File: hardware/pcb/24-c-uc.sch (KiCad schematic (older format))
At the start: 4 parts

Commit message: Changed uC
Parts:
- removed U?: STM32L031K6Tx, Package_QFP:LQFP-32_7x7mm_P0.8mm, symbol MCU_ST_STM32L0:STM32L031K6Tx
- added C? (x3): 100nF, C0603, symbol Device:C
- added U?: STM32L151C8T6, Package_QFP:LQFP-48_7x7mm_P0.5mm, symbol MCU_ST_STM32L1:STM32L151C8Tx
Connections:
- net labels added: uC-Debug-Rx, uC-Debug-Tx
- wire segments 45 -> 85
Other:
- note added: "Add connector for Debug UART"
- note added: "Check caps"
- moved on the sheet: C?

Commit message: Created variants
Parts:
- gave numbers to parts that had none: 7
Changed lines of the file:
@@
 EESchema Schematic File Version 4
-EELAYER 30 0
+LIBS:24-clocks-cache
+EELAYER 29 0
 EELAYER END
 $Descr A4 11693 8268
@@
 P 5250 1400
 AR Path="/5FDEDBF8" Ref="#PWR?"  Part="1"
-AR Path="/5FDEAABE/5FDEDBF8" Ref="#PWR?"  Part="1"
-F 0 "#PWR?" H 5250 1250 50  0001 C CNN
+AR Path="/5FDEAABE/5FDEDBF8" Ref="#PWR0201"  Part="1"
+F 0 "#PWR0201" H 5250 1250 50  0001 C CNN
 F 1 "+3V3" H 5265 1573 50  0000 C CNN
 F 2 "" H 5250 1400 50  0001 C CNN
@@
 P 5250 4800
 AR Path="/5FDEDBFE" Ref="#PWR?"  Part="1"
-AR Path="/5FDEAABE/5FDEDBFE" Ref="#PWR?"  Part="1"
-F 0 "#PWR?" H 5250 4550 50  0001 C CNN
+AR Path="/5FDEAABE/5FDEDBFE" Ref="#PWR0202"  Part="1"
+F 0 "#PWR0202" H 5250 4550 50  0001 C CNN
 F 1 "GND" H 5255 4627 50  0000 C CNN
 F 2 "" H 5250 4800 50  0001 C CNN
@@
 P 4400 6500
 AR Path="/5FDEDC0A" Ref="C?"  Part="1"
-AR Path="/5FDEAABE/5FDEDC0A" Ref="C?"  Part="1"
-F 0 "C?" H 4515 6546 50  0000 L CNN
+AR Path="/5FDEAABE/5FDEDC0A" Ref="C201"  Part="1"
+F 0 "C201" H 4515 6546 50  0000 L CNN
 F 1 "100nF" H 4515 6455 50  0000 L CNN
 F 2 "C0603" H 4438 6350 50  0001 C CNN
@@
 P 4400 6800
 AR Path="/5FDEDC10" Ref="#PWR?"  Part="1"
-AR Path="/5FDEAABE/5FDEDC10" Ref="#PWR?"  Part="1"
-F 0 "#PWR?" H 4400 6550 50  0001 C CNN
+AR Path="/5FDEAABE/5FDEDC10" Ref="#PWR0207"  Part="1"
+F 0 "#PWR0207" H 4400 6550 50  0001 C CNN
 F 1 "GND" H 4405 6627 50  0000 C CNN
 F 2 "" H 4400 6800 50  0001 C CNN
@@
 P 4400 6200
 AR Path="/5FDEDC16" Ref="#PWR?"  Part="1"
-AR Path="/5FDEAABE/5FDEDC16" Ref="#PWR?"  Part="1"
-F 0 "#PWR?" H 4400 6050 50  0001 C CNN
+AR Path="/5FDEAABE/5FDEDC16" Ref="#PWR0204"  Part="1"
+F 0 "#PWR0204" H 4400 6050 50  0001 C CNN
 F 1 "+3V3" H 4415 6373 50  0000 C CNN
 F 2 "" H 4400 6200 50  0001 C CNN
@@
 	4400 6650 4400 6700
 $Comp
-L Connector_Generic:Conn_02x04_Odd_Even J?
+L Connector_Generic:Conn_02x04_Odd_Even J201
 U 1 1 5FDEF68E
 P 2100 6500
-F 0 "J?" H 2150 6817 50  0000 C CNN
+F 0 "J201" H 2150 6817 50  0000 C CNN
 F 1 "ST-LINK" H 2150 6726 50  0000 C CNN
 F 2 "" H 2100 6500 50  0001 C CNN
@@
 P 1850 6800
 AR Path="/5FDF199A" Ref="#PWR?"  Part="1"
-AR Path="/5FDEAABE/5FDF199A" Ref="#PWR?"  Part="1"
-F 0 "#PWR?" H 1850 6550 50  0001 C CNN
+AR Path="/5FDEAABE/5FDF199A" Ref="#PWR0205"  Part="1"
+F 0 "#PWR0205" H 1850 6550 50  0001 C CNN
 F 1 "GND" H 1855 6627 50  0000 C CNN
 F 2 "" H 1850 6800 50  0001 C CNN
@@
 P 2450 6800
 AR Path="/5FDF1E9B" Ref="#PWR?"  Part="1"
-AR Path="/5FDEAABE/5FDF1E9B" Ref="#PWR?"  Part="1"
-F 0 "#PWR?" H 2450 6550 50  0001 C CNN
+AR Path="/5FDEAABE/5FDF1E9B" Ref="#PWR0206"  Part="1"
+F 0 "#PWR0206" H 2450 6550 50  0001 C CNN
 F 1 "GND" H 2455 6627 50  0000 C CNN
 F 2 "" H 2450 6800 50  0001 C CNN
@@
 AR Path="/5FDF3B86" Ref="JP?"  Part="1"
 AR Path="/5FDA43A0/5FDF3B86" Ref="JP?"  Part="1"
-AR Path="/5FDEAABE/5FDF3B86" Ref="JP?"  Part="1"
-F 0 "JP?" H 1750 5971 50  0000 C CNN
+AR Path="/5FDEAABE/5FDF3B86" Ref="JP201"  Part="1"
+F 0 "JP201" H 1750 5971 50  0000 C CNN
 F 1 "Jumper_NC_Small" H 1750 5971 50  0001 C CNN
 F 2 "" H 1750 5850 50  0001 C CNN
@@
 P 1750 5650
 AR Path="/5FDF425C" Ref="#PWR?"  Part="1"
-AR Path="/5FDEAABE/5FDF425C" Ref="#PWR?"  Part="1"
-F 0 "#PWR?" H 1750 5500 50  0001 C CNN
+AR Path="/5FDEAABE/5FDF425C" Ref="#PWR0203"  Part="1"
+F 0 "#PWR0203" H 1750 5500 50  0001 C CNN
 F 1 "+3V3" H 1765 5823 50  0000 C CNN
 F 2 "" H 1750 5650 50  0001 C CNN
@@
 	8800 3750 9400 3750
 $Comp
-L MCU_ST_STM32L1:STM32L151C8Tx U?
+L MCU_ST_STM32L1:STM32L151C8Tx U201
 U 1 1 5FCD10ED
 P 5200 3100
-F 0 "U?" H 4800 4700 50  0000 C CNN
+F 0 "U201" H 4800 4700 50  0000 C CNN
 F 1 "STM32L151C8T6" H 5750 1500 50  0000 C CNN
 F 2 "Package_QFP:LQFP-48_7x7mm_P0.5mm" H 4700 1600 50  0001 R CNN
@@
 P 4900 6500
 AR Path="/5FCE8A85" Ref="C?"  Part="1"
-AR Path="/5FDEAABE/5FCE8A85" Ref="C?"  Part="1"
-F 0 "C?" H 5015 6546 50  0000 L CNN
+AR Path="/5FDEAABE/5FCE8A85" Ref="C202"  Part="1"
+F 0 "C202" H 5015 6546 50  0000 L CNN
 F 1 "100nF" H 5015 6455 50  0000 L CNN
 F 2 "C0603" H 4938 6350 50  0001 C CNN
@@
 P 5400 6500
 AR Path="/5FCEA1E4" Ref="C?"  Part="1"
-AR Path="/5FDEAABE/5FCEA1E4" Ref="C?"  Part="1"
-F 0 "C?" H 5515 6546 50  0000 L CNN
+AR Path="/5FDEAABE/5FCEA1E4" Ref="C203"  Part="1"
+F 0 "C203" H 5515 6546 50  0000 L CNN
 F 1 "100nF" H 5515 6455 50  0000 L CNN
 F 2 "C0603" H 5438 6350 50  0001 C CNN
@@
 P 5900 6500
 AR Path="/5FCEB9CD" Ref="C?"  Part="1"
-AR Path="/5FDEAABE/5FCEB9CD" Ref="C?"  Part="1"
-F 0 "C?" H 6015 6546 50  0000 L CNN
+AR Path="/5FDEAABE/5FCEB9CD" Ref="C204"  Part="1"
+F 0 "C204" H 6015 6546 50  0000 L CNN
 F 1 "100nF" H 6015 6455 50  0000 L CNN
 F 2 "C0603" H 5938 6350 50  0001 C CNN

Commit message: Added debug connector
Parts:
- added J202: Debug UART, symbol Connector_Generic:Conn_01x06
- added JP202: Jumper_NO_Small, symbol Device:Jumper_NO_Small
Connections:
- wire segments 85 -> 90
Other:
- note added: "Debug"
- note added: "Program connector"
- note removed: "Add connector for Debug UART"
- moved on the sheet: C201, C202, C203, C204, J201, JP201

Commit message: Changed uC
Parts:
- removed U201: STM32L151C8T6, Package_QFP:LQFP-48_7x7mm_P0.5mm, symbol MCU_ST_STM32L1:STM32L151C8Tx
- added C205, C206: 20pF, symbol Device:C
- added JP203: Jumper_NO_Small, symbol Device:Jumper_NO_Small
- added U201: STM32F103C8Tx, Package_QFP:LQFP-48_7x7mm_P0.5mm, symbol MCU_ST_STM32F1:STM32F103C8Tx
- added Y201: 8MHz, symbol Device:Crystal
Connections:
- net labels removed: SWCLK
- wire segments 90 -> 106
- no-connect marks 0 -> 20

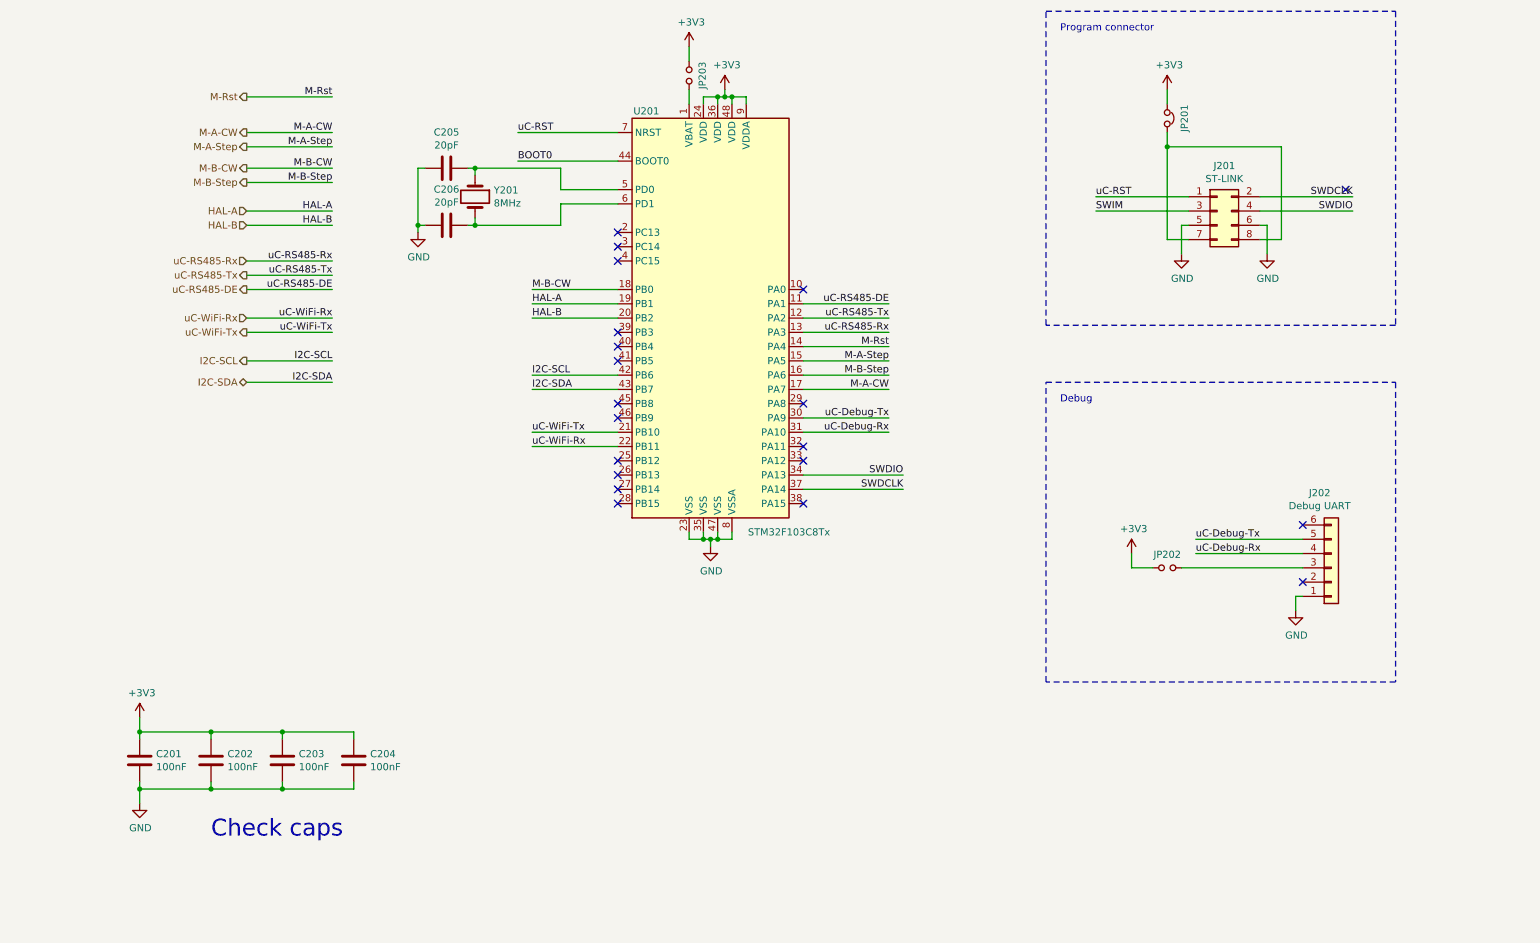
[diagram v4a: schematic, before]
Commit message: Updated processor pins and added testpoints
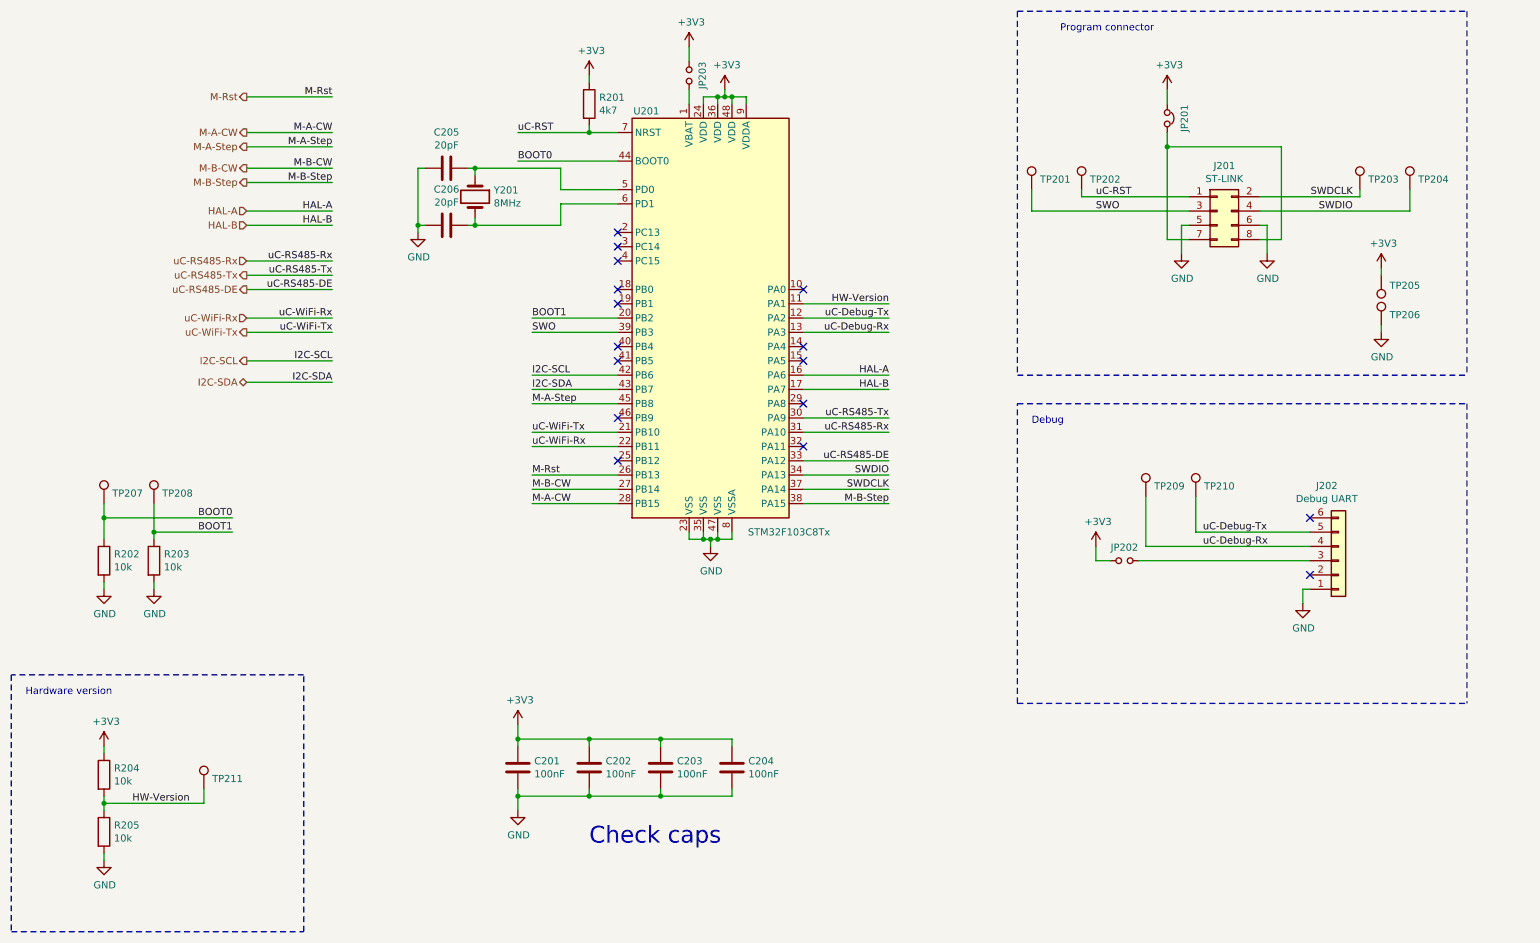
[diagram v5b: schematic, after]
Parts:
- added R201: 4k7, Resistor_SMD:R_0603_1608Metric, symbol Device:R
- added R202, R203, R204, R205: 10k, Resistor_SMD:R_0603_1608Metric, symbol Device:R
- added TP201: SWO, symbol Connector:TestPoint
- added TP202: uC-Rst, symbol Connector:TestPoint
- added TP203: SWDCLK, symbol Connector:TestPoint
- added TP204: SWDIO, symbol Connector:TestPoint
- added TP205: 3V3, symbol Connector:TestPoint
- added TP206: GND, symbol Connector:TestPoint
- added TP207: BOOT0, symbol Connector:TestPoint
- added TP208: BOOT1, symbol Connector:TestPoint
- added TP209: uC-Debug-Rx, symbol Connector:TestPoint
- added TP210: uC-Debug-Tx, symbol Connector:TestPoint
- added TP211: HW-Version, symbol Connector:TestPoint
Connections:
- net SWIM is gone; now on net SWO: J201.3 (Pin_3)
- net +3V3: now also R201.1, R204.1, TP205.1
- net BOOT0: now also R202.1, TP207.1
- net GND: now also R202.2, R203.2, R205.2, TP206.1
- net HAL-A: now also U201.16 (PA6); no longer U201.19 (PB1)
- net HAL-B: now also U201.17 (PA7); no longer U201.20 (PB2)
- net M-A-CW: now also U201.28 (PB15); no longer U201.17 (PA7)
- net M-A-Step: now also U201.45 (PB8); no longer U201.15 (PA5)
- net M-B-CW: now also U201.27 (PB14); no longer U201.18 (PB0)
- net M-B-Step: now also U201.38 (PA15); no longer U201.16 (PA6)
- net M-Rst: now also U201.26 (PB13); no longer U201.14 (PA4)
- net SWDCLK: now also TP203.1
- net SWDIO: now also TP204.1
- net uC-Debug-Rx: now also U201.13 (PA3), TP209.1; no longer U201.31 (PA10)
- net uC-Debug-Tx: now also U201.12 (PA2), TP210.1; no longer U201.30 (PA9)
- net uC-RS485-DE: now also U201.33 (PA12); no longer U201.11 (PA1)
- net uC-RS485-Rx: now also U201.31 (PA10); no longer U201.13 (PA3)
- net uC-RS485-Tx: now also U201.30 (PA9); no longer U201.12 (PA2)
- net uC-RST: now also R201.2, TP202.1
- net SWO: now reaches U201.39 (PB3)
- net SWO: now also TP201.1
- new net BOOT1: R203.1, TP208.1, U201.20 (PB2)
- new net HW-Version: R204.2, R205.1, TP211.1, U201.11 (PA1)
- no-connect marks 20 -> 16
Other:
- note added: "Hardware version"
- moved on the sheet: C201, C202, C203, C204, J202, JP202

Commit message: Updated footprints
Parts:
- C201, C202, C203, C204: footprint C0603 -> Capacitor_SMD:C_0603_1608Metric
- C205, C206: footprint (none) -> Capacitor_SMD:C_0603_1608Metric
- J201: footprint (none) -> Connector_PinHeader_2.54mm:PinHeader_2x04_P2.54mm_Vertical
- J202: footprint (none) -> Connector_PinHeader_2.54mm:PinHeader_1x06_P2.54mm_Vertical
- JP201: footprint (none) -> Jumper:SolderJumper-2_P1.3mm_Bridged_RoundedPad1.0x1.5mm
- JP202, JP203: footprint (none) -> Jumper:SolderJumper-2_P1.3mm_Open_RoundedPad1.0x1.5mm
- TP201, TP202, TP203, TP204, TP205, TP206, TP207, TP208, TP209, TP210, TP211: footprint (none) -> TestPoint:TestPoint_Pad_1.5x1.5mm
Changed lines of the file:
@@
 F 0 "C201" H 4415 6396 50  0000 L CNN
 F 1 "100nF" H 4415 6305 50  0000 L CNN
-F 2 "C0603" H 4338 6200 50  0001 C CNN
+F 2 "Capacitor_SMD:C_0603_1608Metric" H 4338 6200 50  0001 C CNN
 F 3 "~" H 4300 6350 50  0001 C CNN
 	1    4300 6350
@@
 F 0 "J201" H 9250 2767 50  0000 C CNN
 F 1 "ST-LINK" H 9250 2676 50  0000 C CNN
-F 2 "" H 9200 2450 50  0001 C CNN
+F 2 "Connector_PinHeader_2.54mm:PinHeader_2x04_P2.54mm_Vertical" H 9200 2450 50  0001 C CNN
 F 3 "~" H 9200 2450 50  0001 C CNN
 	1    9200 2450
@@
 F 0 "JP201" H 8850 1921 50  0000 C CNN
 F 1 "Jumper_NC_Small" H 8850 1921 50  0001 C CNN
-F 2 "" H 8850 1800 50  0001 C CNN
+F 2 "Jumper:SolderJumper-2_P1.3mm_Bridged_RoundedPad1.0x1.5mm" H 8850 1800 50  0001 C CNN
 F 3 "~" H 8850 1800 50  0001 C CNN
 	1    8850 1800
@@
 F 0 "C202" H 4915 6396 50  0000 L CNN
 F 1 "100nF" H 4915 6305 50  0000 L CNN
-F 2 "C0603" H 4838 6200 50  0001 C CNN
+F 2 "Capacitor_SMD:C_0603_1608Metric" H 4838 6200 50  0001 C CNN
 F 3 "~" H 4800 6350 50  0001 C CNN
 	1    4800 6350
@@
 F 0 "C203" H 5415 6396 50  0000 L CNN
 F 1 "100nF" H 5415 6305 50  0000 L CNN
-F 2 "C0603" H 5338 6200 50  0001 C CNN
+F 2 "Capacitor_SMD:C_0603_1608Metric" H 5338 6200 50  0001 C CNN
 F 3 "~" H 5300 6350 50  0001 C CNN
 	1    5300 6350
@@
 F 0 "C204" H 5915 6396 50  0000 L CNN
 F 1 "100nF" H 5915 6305 50  0000 L CNN
-F 2 "C0603" H 5838 6200 50  0001 C CNN
+F 2 "Capacitor_SMD:C_0603_1608Metric" H 5838 6200 50  0001 C CNN
 F 3 "~" H 5800 6350 50  0001 C CNN
 	1    5800 6350
@@
 F 0 "J202" H 9968 4375 50  0000 C CNN
 F 1 "Debug UART" H 9968 4466 50  0000 C CNN
-F 2 "" H 10050 4900 50  0001 C CNN
+F 2 "Connector_PinHeader_2.54mm:PinHeader_1x06_P2.54mm_Vertical" H 10050 4900 50  0001 C CNN
 F 3 "~" H 10050 4900 50  0001 C CNN
 	1    10050 4900
@@
 F 0 "JP202" H 8550 4993 50  0000 C CNN
 F 1 "Jumper_NO_Small" H 8550 4994 50  0001 C CNN
-F 2 "" H 8550 4900 50  0001 C CNN
+F 2 "Jumper:SolderJumper-2_P1.3mm_Open_RoundedPad1.0x1.5mm" H 8550 4900 50  0001 C CNN
 F 3 "~" H 8550 4900 50  0001 C CNN
 	1    8550 4900
@@
 F 0 "C205" V 3548 2150 50  0000 C CNN
 F 1 "20pF" V 3639 2150 50  0000 C CNN
-F 2 "" H 3838 2000 50  0001 C CNN
+F 2 "Capacitor_SMD:C_0603_1608Metric" H 3838 2000 50  0001 C CNN
 F 3 "~" H 3800 2150 50  0001 C CNN
 	1    3800 2150
@@
 F 0 "C206" V 3548 2550 50  0000 C CNN
 F 1 "20pF" V 3639 2550 50  0000 C CNN
-F 2 "" H 3838 2400 50  0001 C CNN
+F 2 "Capacitor_SMD:C_0603_1608Metric" H 3838 2400 50  0001 C CNN
 F 3 "~" H 3800 2550 50  0001 C CNN
 	1    3800 2550
@@
 F 0 "JP203" H 5500 1593 50  0000 C CNN
 F 1 "Jumper_NO_Small" H 5500 1594 50  0001 C CNN
-F 2 "" H 5500 1500 50  0001 C CNN
+F 2 "Jumper:SolderJumper-2_P1.3mm_Open_RoundedPad1.0x1.5mm" H 5500 1500 50  0001 C CNN
 F 3 "~" H 5500 1500 50  0001 C CNN
 	1    5500 1500
@@
 F 0 "TP207" H 1458 4572 50  0000 L CNN
 F 1 "BOOT0" H 1458 4527 50  0001 L CNN
-F 2 "" H 1600 4500 50  0001 C CNN
+F 2 "TestPoint:TestPoint_Pad_1.5x1.5mm" H 1600 4500 50  0001 C CNN
 F 3 "~" H 1600 4500 50  0001 C CNN
 	1    1400 4500
@@
 F 0 "TP208" H 1808 4572 50  0000 L CNN
 F 1 "BOOT1" H 1808 4527 50  0001 L CNN
-F 2 "" H 1950 4500 50  0001 C CNN
+F 2 "TestPoint:TestPoint_Pad_1.5x1.5mm" H 1950 4500 50  0001 C CNN
 F 3 "~" H 1950 4500 50  0001 C CNN
 	1    1750 4500
@@
 F 0 "TP202" H 8308 2372 50  0000 L CNN
 F 1 "uC-Rst" H 8308 2327 50  0001 L CNN
-F 2 "" H 8450 2300 50  0001 C CNN
+F 2 "TestPoint:TestPoint_Pad_1.5x1.5mm" H 8450 2300 50  0001 C CNN
 F 3 "~" H 8450 2300 50  0001 C CNN
 	1    8250 2300
@@
 F 0 "TP201" H 7958 2372 50  0000 L CNN
 F 1 "SWO" H 7958 2327 50  0001 L CNN
-F 2 "" H 8100 2300 50  0001 C CNN
+F 2 "TestPoint:TestPoint_Pad_1.5x1.5mm" H 8100 2300 50  0001 C CNN
 F 3 "~" H 8100 2300 50  0001 C CNN
 	1    7900 2300
@@
 F 0 "TP206" H 10408 3322 50  0000 L CNN
 F 1 "GND" H 10408 3277 50  0001 L CNN
-F 2 "" H 10550 3250 50  0001 C CNN
+F 2 "TestPoint:TestPoint_Pad_1.5x1.5mm" H 10550 3250 50  0001 C CNN
 F 3 "~" H 10550 3250 50  0001 C CNN
 	1    10350 3250
@@
 F 0 "TP205" H 10292 2972 50  0000 R CNN
 F 1 "3V3" H 10408 2927 50  0001 L CNN
-F 2 "" H 10550 2900 50  0001 C CNN
+F 2 "TestPoint:TestPoint_Pad_1.5x1.5mm" H 10550 2900 50  0001 C CNN
 F 3 "~" H 10550 2900 50  0001 C CNN
 	1    10350 2900
@@
 F 0 "TP203" H 10258 2372 50  0000 L CNN
 F 1 "SWDCLK" H 10258 2327 50  0001 L CNN
-F 2 "" H 10400 2300 50  0001 C CNN
+F 2 "TestPoint:TestPoint_Pad_1.5x1.5mm" H 10400 2300 50  0001 C CNN
 F 3 "~" H 10400 2300 50  0001 C CNN
 	1    10200 2300
@@
 F 0 "TP204" H 10608 2372 50  0000 L CNN
 F 1 "SWDIO" H 10608 2327 50  0001 L CNN
-F 2 "" H 10750 2300 50  0001 C CNN
+F 2 "TestPoint:TestPoint_Pad_1.5x1.5mm" H 10750 2300 50  0001 C CNN
 F 3 "~" H 10750 2300 50  0001 C CNN
 	1    10550 2300
@@
 F 0 "TP210" H 9108 4522 50  0000 L CNN
 F 1 "uC-Debug-Tx" H 9108 4477 50  0001 L CNN
-F 2 "" H 9250 4450 50  0001 C CNN
+F 2 "TestPoint:TestPoint_Pad_1.5x1.5mm" H 9250 4450 50  0001 C CNN
 F 3 "~" H 9250 4450 50  0001 C CNN
 	1    9050 4450
@@
 F 0 "TP209" H 8758 4522 50  0000 L CNN
 F 1 "uC-Debug-Rx" H 8758 4477 50  0001 L CNN
-F 2 "" H 8900 4450 50  0001 C CNN
+F 2 "TestPoint:TestPoint_Pad_1.5x1.5mm" H 8900 4450 50  0001 C CNN
 F 3 "~" H 8900 4450 50  0001 C CNN
 	1    8700 4450
@@
 F 0 "TP211" H 2158 6572 50  0000 L CNN
 F 1 "HW-Version" H 2158 6527 50  0001 L CNN
-F 2 "" H 2300 6500 50  0001 C CNN
+F 2 "TestPoint:TestPoint_Pad_1.5x1.5mm" H 2300 6500 50  0001 C CNN
 F 3 "~" H 2300 6500 50  0001 C CNN
 	1    2100 6500
